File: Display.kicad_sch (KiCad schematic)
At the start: 41 parts, among them J14 LCD_TP_I2C, J2 TFT_LCD, J4 SPI_LCD, U3 MT9284, U5 TPS61169

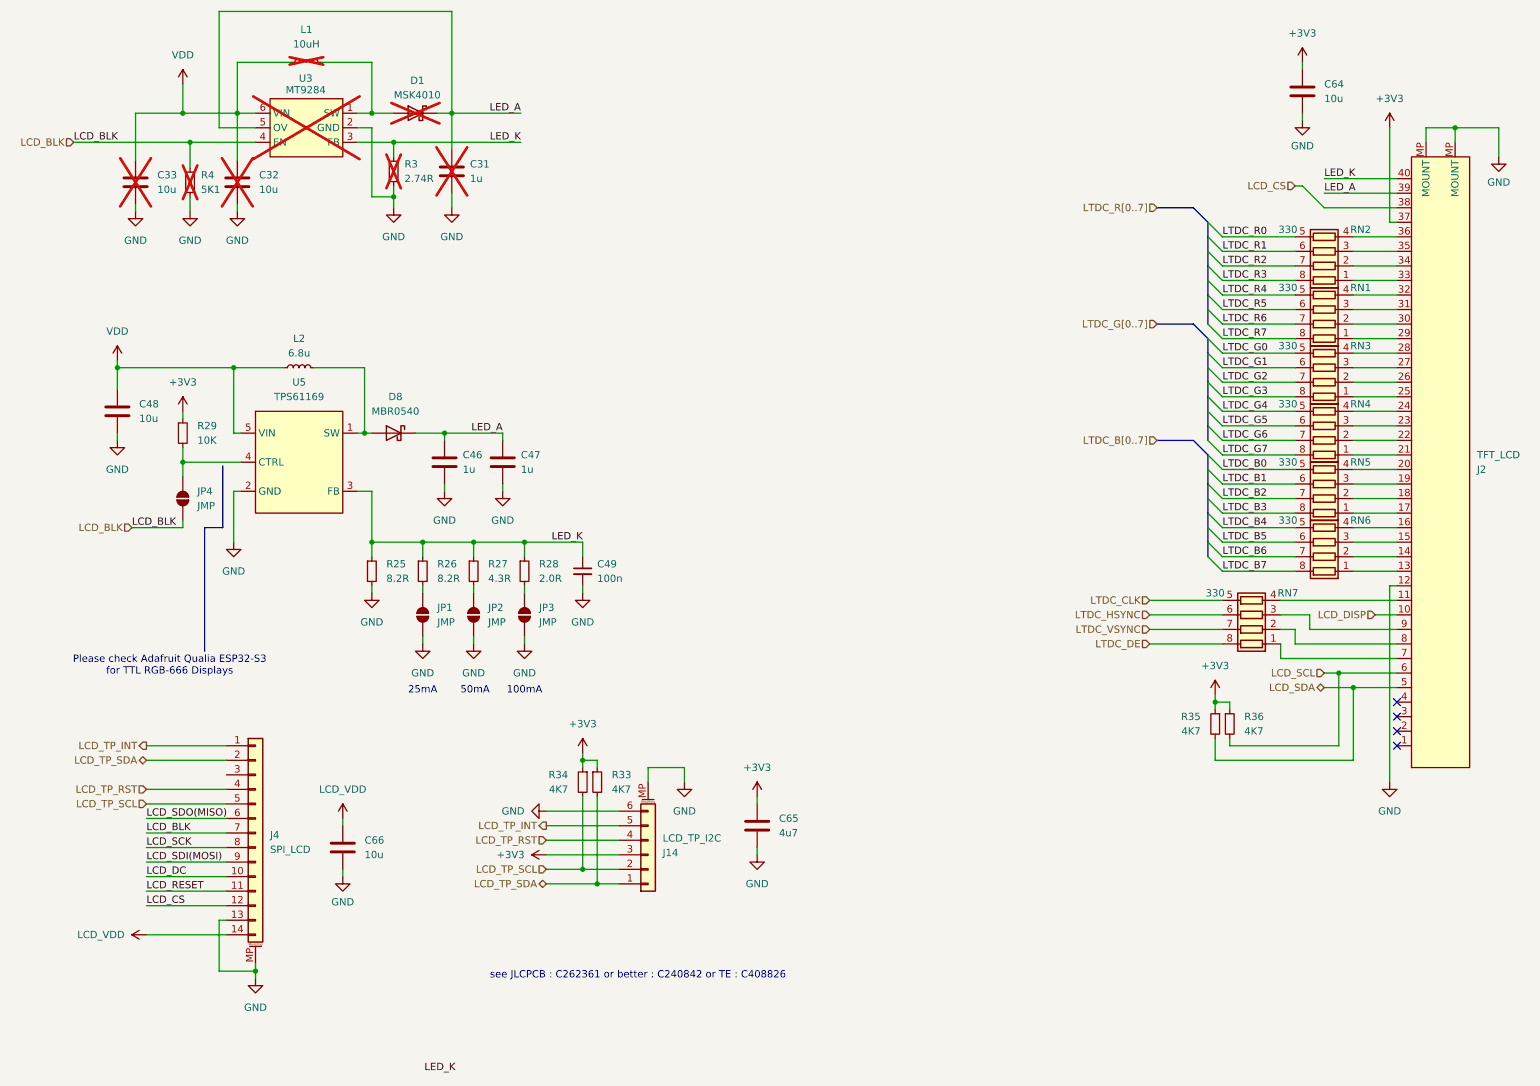
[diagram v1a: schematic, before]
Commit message: Button, LED, i2s audio, LCD & SD ctrl left
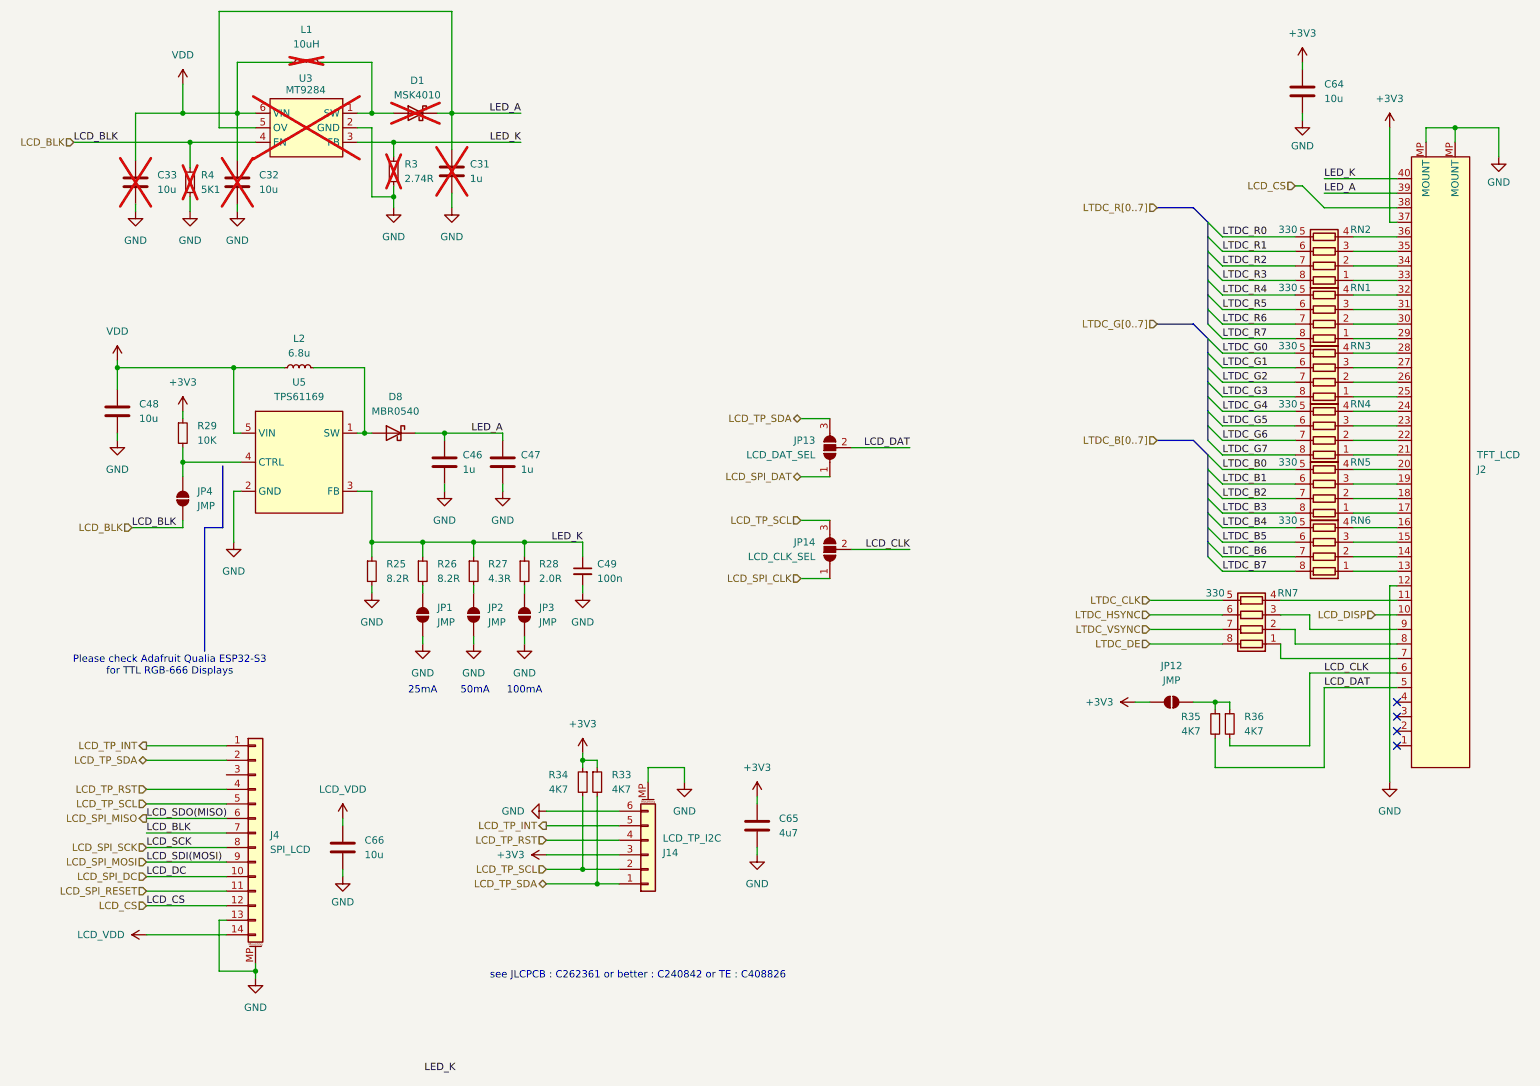
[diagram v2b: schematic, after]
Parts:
- added JP12: JMP, Jumper:SolderJumper-2_P1.3mm_Open_RoundedPad1.0x1.5mm, symbol Jumper:SolderJumper_2_Open
- added JP13: LCD_DAT_SEL, Jumper:SolderJumper-3_P1.3mm_Open_RoundedPad1.0x1.5mm_NumberLabels, symbol Jumper:SolderJumper_3_Open
- added JP14: LCD_CLK_SEL, Jumper:SolderJumper-3_P1.3mm_Open_RoundedPad1.0x1.5mm_NumberLabels, symbol Jumper:SolderJumper_3_Open
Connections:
- net +3V3: now also JP12.2 (B); no longer R35.1, R36.1
- net LCD_TP_SCL: now also JP14.3 (B)
- net LCD_TP_SDA: now also JP13.3 (B)
- net LCD_DC renamed LCD_SPI_DC
- net LCD_RESET renamed LCD_SPI_RESET
- net LCD_SCK renamed LCD_SPI_SCK
- net LCD_SCL renamed LCD_CLK
- net LCD_CLK: now also JP14.2 (C)
- net LCD_SDA renamed LCD_DAT
- net LCD_DAT: now also JP13.2 (C)
- net LCD_SDI(MOSI) renamed LCD_SPI_MOSI
- net LCD_SDO(MISO) renamed LCD_SPI_MISO
- new net: JP12.1 (A), R35.1, R36.1
- new net LCD_SPI_CLK: JP14.1 (A)
- new net LCD_SPI_DAT: JP13.1 (A)

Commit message: Almost finished
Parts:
- C65: JLCPCB Part # C96446 -> C19666
- RN1, RN2, RN3, RN4, RN5, RN6, RN7: JLCPCB Part # (none) -> C12018
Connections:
- net LCD_CS: no longer J4.12 (Pin_12)
- new net LCD_SPI_CS: J4.12 (Pin_12)
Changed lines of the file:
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@@
 		)
 	)
-	(label "LCD_CS"
-		(at 40.64 175.26 0)
-		(fields_autoplaced yes)
-		(effects
-			(font
-				(size 1.27 1.27)
-			)
-			(justify left bottom)
-		)
-	)
 	(hierarchical_label "LCD_BLK"
 		(shape input)
@@
 		)
 	)
-	(hierarchical_label "LCD_CS"
-		(shape input)
-		(at 40.64 175.26 180)
-		(fields_autoplaced yes)
-		(effects
-			(font
-				(size 1.27 1.27)
-			)
-			(justify right)
-		)
-	)
 	(hierarchical_label "LCD_SPI_MISO"
 		(shape output)
@@
 		)
 	)
+	(hierarchical_label "LCD_SPI_CS"
+		(shape input)
+		(at 40.64 175.26 180)
+		(fields_autoplaced yes)
+		(effects
+			(font
+				(size 1.27 1.27)
+			)
+			(justify right)
+		)
+	)
 	(hierarchical_label "LCD_BLK"
 		(shape input)
@@
 			)
 		)
+		(property "JLCPCB Part #" "C12018"
+			(at 246.38 101.6 0)
+			(effects
+				(font
+					(size 1.27 1.27)
+				)
+				(hide yes)
+			)
+		)
 		(pin "1"
 		)
@@
 			)
 		)
+		(property "JLCPCB Part #" "C12018"
+			(at 246.38 111.76 0)
+			(effects
+				(font
+					(size 1.27 1.27)
+				)
+				(hide yes)
+			)
+		)
 		(pin "1"
 		)
@@
 			)
 		)
+		(property "JLCPCB Part #" "C12018"
+			(at 246.38 81.28 0)
+			(effects
+				(font
+					(size 1.27 1.27)
+				)
+				(hide yes)
+			)
+		)
 		(pin "1"
 		)
@@
 			)
 		)
+		(property "JLCPCB Part #" "C12018"
+			(at 246.38 91.44 0)
+			(effects
+				(font
+					(size 1.27 1.27)
+				)
+				(hide yes)
+			)
+		)
 		(pin "1"
 		)
@@
 			)
 		)
-		(property "JLCPCB Part #" "C96446"
+		(property "JLCPCB Part #" "C19666 "
 			(at 147.32 161.29 0)
 			(effects
@@
 			)
 		)
+		(property "JLCPCB Part #" "C12018"
+			(at 246.38 60.96 0)
+			(effects
+				(font
+					(size 1.27 1.27)
+				)
+				(hide yes)
+			)
+		)
 		(pin "1"
 		)
@@
 			)
 		)
+		(property "JLCPCB Part #" "C12018"
+			(at 246.38 71.12 0)
+			(effects
+				(font
+					(size 1.27 1.27)
+				)
+				(hide yes)
+			)
+		)
 		(pin "1"
 		)
@@
 			(at 233.68 124.46 0)
 			(effects
+				(font
+					(size 1.27 1.27)
+				)
+				(hide yes)
+			)
+		)
+		(property "JLCPCB Part #" "C12018"
+			(at 233.68 124.46 0)
+			(effects

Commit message: Still on progress...
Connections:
- net +3V3: no longer C64.1, C65.1, J14.3 (Pin_3), J2.37
- net LCD_VDD renamed +3V3A
- net +3V3A: now also C64.1, C65.1, J14.3 (Pin_3), J2.37
- no-connect marks 4 -> 5

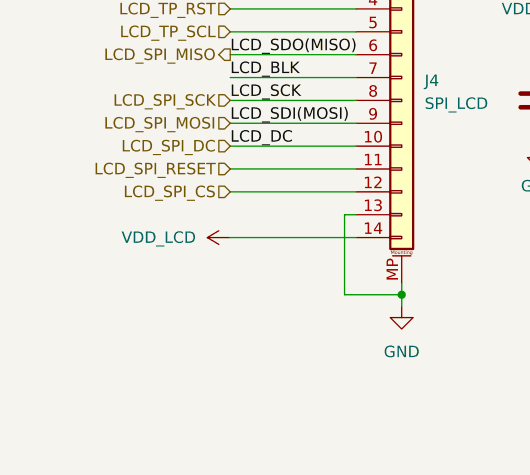
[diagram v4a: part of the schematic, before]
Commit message: Removing Camera, create alternative footprint for SPI LCD conn
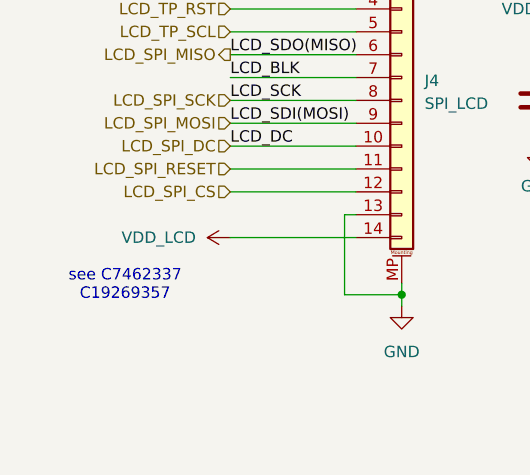
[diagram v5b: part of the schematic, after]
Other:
- note added: "see C7462337 C19269357"
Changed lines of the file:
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@@
+		)
+	)
+	(text "see C7462337\nC19269357"
+		(exclude_from_sim no)
+		(at 28.956 185.674 0)
+		(effects
+			(font
+				(size 1.27 1.27)
+			)
 		)
 	)

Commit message: First release
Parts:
- added TP5, TP6, TP7: TestPoint, TestPoint:TestPoint_Pad_D1.5mm, symbol Connector:TestPoint
- C65: JLCPCB Part # C19666 -> C19666
- J4: footprint Connector_FFC-FPC:TE_1-84953-4_1x14-1MP_P1.0mm_Horizontal -> FPC-custom:FPC-14P-1mm-XUNPU; JLCPCB Part # (none) -> C19269357
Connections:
- net +3V3A: now also J4.1 (Pin_1); no longer J4.14 (Pin_14)
- net GND: now also J4.2 (Pin_2), TP7.1; no longer J4.13 (Pin_13)
- net LCD_BLK: now also J4.8 (Pin_8); no longer J4.7 (Pin_7)
- net LCD_SPI_CS: now also J4.3 (Pin_3); no longer J4.12 (Pin_12)
- net LCD_SPI_DC: now also J4.5 (Pin_5); no longer J4.10 (Pin_10)
- net LCD_SPI_MISO: now also J4.9 (Pin_9); no longer J4.6 (Pin_6)
- net LCD_SPI_MOSI: now also J4.6 (Pin_6); no longer J4.9 (Pin_9)
- net LCD_SPI_RESET: now also J4.4 (Pin_4); no longer J4.11 (Pin_11)
- net LCD_SPI_SCK: now also J4.7 (Pin_7); no longer J4.8 (Pin_8)
- net LCD_TP_INT: now also J4.14 (Pin_14); no longer J4.1 (Pin_1)
- net LCD_TP_RST: now also J4.11 (Pin_11); no longer J4.4 (Pin_4)
- net LCD_TP_SCL: now also J4.10 (Pin_10); no longer J4.5 (Pin_5)
- net LCD_TP_SDA: now also J4.13 (Pin_13); no longer J4.2 (Pin_2)
- net LED_A: now also TP5.1
- net LED_K: now also TP6.1
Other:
- moved on the sheet: J4
